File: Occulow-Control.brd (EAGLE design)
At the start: 38.1 x 101.6 mm, 40 parts, among them T1 DMP3010LK3, T2 DMP3010LK3, T3 DMP3010LK3

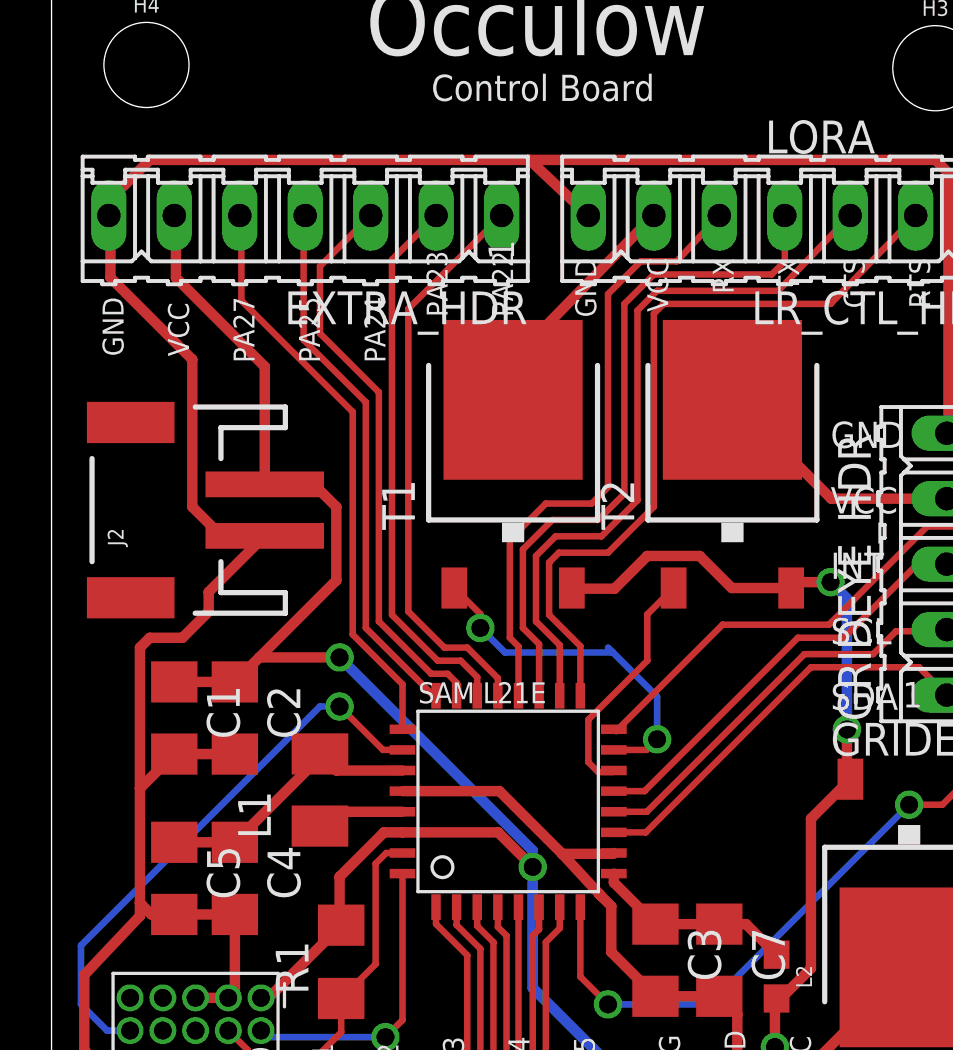
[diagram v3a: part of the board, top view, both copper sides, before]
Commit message: Added LED status, bom. Fixes #6"
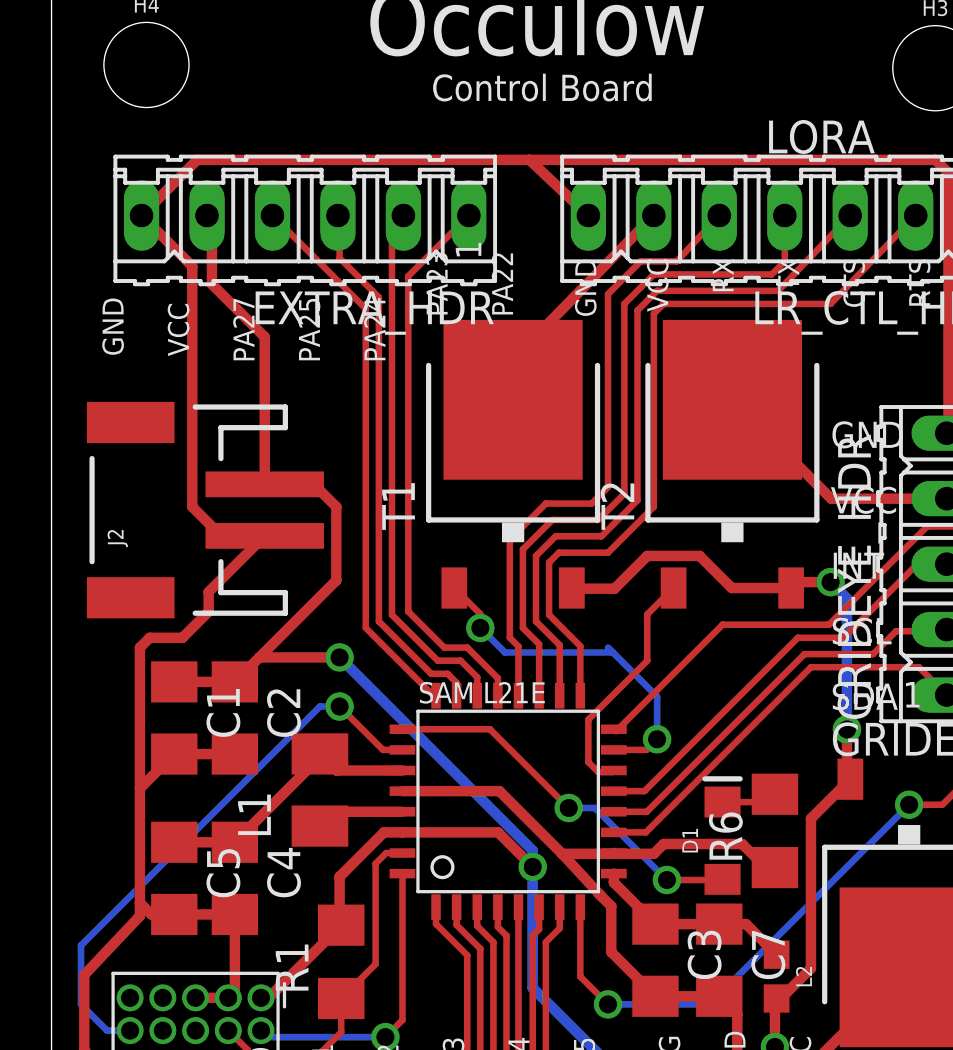
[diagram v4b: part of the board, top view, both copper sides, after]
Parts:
- added D1: (no value), SparkFun-LED:LED-1206
- added R6: 330, resistor:R1206
- EXTRA_HDR: device con-amp-quick:07P -> con-amp-quick:06P
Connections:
- new net N$1: D1.C, R6.2
- net GND: now also EXTRA_HDR.6, R6.1; no longer EXTRA_HDR.7
- net PA27: now also D1.A; no longer EXTRA_HDR.5
- net VCC: now also EXTRA_HDR.5; no longer EXTRA_HDR.6
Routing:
- net PA27: track 22.5 -> 14.9 mm, vias 0 -> 2
- net GND: track 155.6 -> 160.3 mm
- net N$1: track 0.00 -> 2.16 mm
- net PA24: track 22.0 -> 20.9 mm
- net PA25: track 20.8 -> 21.6 mm
- net PA23: track 21.2 -> 20.7 mm
- net VCC: track 101.6 -> 101.1 mm
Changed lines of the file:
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@@
 </element>
 <element name="R1" library="resistor" package="R1206" value="1k" x="11.2395" y="11.049" rot="R90"/>
-<element name="EXTRA_HDR" library="con-amp-quick" package="07P" value="" x="9.8425" y="40.005" rot="R180">
+<element name="EXTRA_HDR" library="con-amp-quick" package="06P" value="" x="9.8425" y="40.005" rot="R180">
 <attribute name="MF" value="" x="9.8425" y="40.005" size="1.778" layer="27" rot="R180" display="off"/>
 <attribute name="MPN" value="" x="9.8425" y="40.005" size="1.778" layer="27" rot="R180" display="off"/>
@@
 </element>
 <element name="U$5" library="cortex-debug" package="2X5-1.27MM" value="CORTEX-ICE" x="5.588" y="9.652" rot="R180"/>
+<element name="D1" library="SparkFun-LED" package="LED-1206" value="" x="26.035" y="15.748" rot="R90"/>
+<element name="R6" library="resistor" package="R1206" value="330" x="28.067" y="16.129" rot="R90"/>
 </elements>
 <signals>
@@
 <contactref element="C1" pad="2"/>
 <contactref element="C2" pad="2"/>
-<contactref element="EXTRA_HDR" pad="7"/>
 <contactref element="C4" pad="2"/>
 <contactref element="C5" pad="2"/>
@@
 <wire x1="17.38" y1="17.672" x2="19.812" y2="15.24" width="0.4064" layer="1"/>
 <wire x1="19.812" y1="15.24" x2="21.7845" y2="15.24" width="0.4064" layer="1"/>
-<wire x1="21.7845" y1="15.24" x2="21.8165" y2="15.272" width="0.4064" layer="1"/>
+<wire x1="21.8165" y1="15.272" x2="21.7845" y2="15.24" width="0.4064" layer="1"/>
 <wire x1="19.812" y1="15.24" x2="21.262965625" y2="13.668121875" width="0.4064" layer="1"/>
 <wire x1="21.262965625" y1="13.668121875" x2="21.336" y2="13.589" width="0.4064" layer="1"/>
@@
 <wire x1="8.272" y1="27.575" x2="6.588" y2="27.575" width="0.4064" layer="1"/>
 <wire x1="6.588" y1="27.575" x2="5.461" y2="28.702" width="0.4064" layer="1"/>
-<wire x1="5.461" y1="28.702" x2="5.461" y2="34.417" width="0.4064" layer="1"/>
-<wire x1="5.461" y1="34.417" x2="2.286" y2="37.592" width="0.4064" layer="1"/>
-<wire x1="2.286" y1="37.592" x2="2.286" y2="39.9415" width="0.4064" layer="1"/>
-<wire x1="2.286" y1="39.9415" x2="2.2225" y2="40.005" width="0.4064" layer="1"/>
-<wire x1="2.2225" y1="40.005" x2="2.2225" y2="40.5765" width="0.4064" layer="1"/>
-<wire x1="2.2225" y1="40.5765" x2="3.81" y2="42.164" width="0.4064" layer="1"/>
-<wire x1="3.81" y1="42.164" x2="18.542" y2="42.164" width="0.4064" layer="1"/>
-<wire x1="18.542" y1="42.164" x2="20.828" y2="40.005" width="0.4064" layer="1"/>
+<wire x1="20.828" y1="40.005" x2="18.542" y2="42.164" width="0.4064" layer="1"/>
 <wire x1="3.429" y1="13.335" x2="3.429" y2="12.827" width="0.4064" layer="1"/>
 <wire x1="3.429" y1="12.827" x2="1.27" y2="10.541" width="0.4064" layer="1"/>
@@
 <wire x1="7.112" y1="9.906" x2="6.858" y2="9.652" width="0.4064" layer="1"/>
 <wire x1="6.858" y1="9.652" x2="5.588" y2="9.652" width="0.4064" layer="1"/>
+<contactref element="R6" pad="1"/>
+<contactref element="EXTRA_HDR" pad="6"/>
+<wire x1="28.067" y1="14.707" x2="27.711" y2="14.707" width="0.4064" layer="1"/>
+<wire x1="27.711" y1="14.707" x2="26.797" y2="15.621" width="0.4064" layer="1"/>
+<wire x1="26.797" y1="15.621" x2="23.749" y2="15.621" width="0.4064" layer="1"/>
+<wire x1="23.749" y1="15.621" x2="23.368" y2="15.24" width="0.4064" layer="1"/>
+<wire x1="23.368" y1="15.24" x2="21.8485" y2="15.24" width="0.4064" layer="1"/>
+<wire x1="21.8485" y1="15.24" x2="21.8165" y2="15.272" width="0.4064" layer="1"/>
+<wire x1="3.4925" y1="40.005" x2="5.461" y2="38.0365" width="0.4064" layer="1"/>
+<wire x1="5.461" y1="28.702" x2="5.461" y2="38.0365" width="0.4064" layer="1"/>
+<wire x1="18.542" y1="42.164" x2="5.6515" y2="42.164" width="0.4064" layer="1"/>
+<wire x1="5.6515" y1="42.164" x2="3.4925" y2="40.005" width="0.4064" layer="1"/>
 </signal>
 <signal name="VCC">
@@
 <contactref element="U$1" pad="30"/>
 <contactref element="C2" pad="1"/>
-<contactref element="EXTRA_HDR" pad="6"/>
 <wire x1="7.112" y1="21.9105" x2="4.7625" y2="21.9105" width="0.4064" layer="1"/>
-<wire x1="8.272" y1="34.146" x2="8.272" y2="29.575" width="0.4064" layer="1"/>
-<wire x1="8.272" y1="34.146" x2="4.826" y2="37.592" width="0.4064" layer="1"/>
-<wire x1="4.826" y1="37.592" x2="4.826" y2="39.9415" width="0.4064" layer="1"/>
-<wire x1="4.826" y1="39.9415" x2="4.7625" y2="40.005" width="0.4064" layer="1"/>
 <wire x1="17.329" y1="16.072" x2="13.6165" y2="16.072" width="0.4064" layer="1"/>
 <wire x1="17.329" y1="16.072" x2="18.669" y2="14.732" width="0.4064" layer="1"/>
@@
 <wire x1="29.464" y1="10.795" x2="29.464" y2="16.605" width="0.4064" layer="1"/>
 <wire x1="30.994" y1="18.135" x2="29.464" y2="16.605" width="0.4064" layer="1"/>
-<wire x1="8.272" y1="29.575" x2="10.176" y2="29.575" width="0.4064" layer="1"/>
+<wire x1="10.176" y1="29.575" x2="8.272" y2="29.575" width="0.4064" layer="1"/>
 <wire x1="10.176" y1="29.575" x2="11.049" y2="28.702" width="0.4064" layer="1"/>
 <wire x1="11.049" y1="28.702" x2="11.049" y2="25.8475" width="0.4064" layer="1"/>
@@
 <wire x1="11.176" y1="22.86" x2="8.0615" y2="22.86" width="0.4064" layer="1"/>
 <wire x1="18.669" y1="15.367" x2="11.176" y2="22.86" width="0.4064" layer="16"/>
+<contactref element="EXTRA_HDR" pad="5"/>
+<wire x1="8.272" y1="35.289" x2="6.223" y2="37.338" width="0.4064" layer="1"/>
+<wire x1="6.223" y1="37.338" x2="6.223" y2="39.8145" width="0.4064" layer="1"/>
+<wire x1="6.223" y1="39.8145" x2="6.0325" y2="40.005" width="0.4064" layer="1"/>
+<wire x1="8.272" y1="29.575" x2="8.272" y2="35.289" width="0.4064" layer="1"/>
 </signal>
 <signal name="RF">
@@
 <wire x1="16.129" y1="23.241" x2="15.24" y2="23.241" width="0.254" layer="1"/>
 <wire x1="15.24" y1="23.241" x2="13.843" y2="24.638" width="0.254" layer="1"/>
-<wire x1="13.843" y1="24.638" x2="13.843" y2="36.3855" width="0.254" layer="1"/>
-<wire x1="13.843" y1="36.3855" x2="17.4625" y2="40.005" width="0.254" layer="1"/>
+<wire x1="13.843" y1="24.638" x2="13.843" y2="36.322" width="0.254" layer="1"/>
+<wire x1="13.843" y1="36.322" x2="13.843" y2="36.3855" width="0.254" layer="1"/>
+<wire x1="13.843" y1="36.322" x2="13.843" y2="37.6555" width="0.254" layer="1"/>
+<wire x1="13.843" y1="37.6555" x2="16.1925" y2="40.005" width="0.254" layer="1"/>
 </signal>
 <signal name="PA23">
@@
 <wire x1="15.875" y1="22.733" x2="14.986" y2="22.733" width="0.254" layer="1"/>
 <wire x1="14.986" y1="22.733" x2="13.208" y2="24.511" width="0.254" layer="1"/>
-<wire x1="13.208" y1="24.511" x2="13.208" y2="38.2905" width="0.254" layer="1"/>
-<wire x1="13.208" y1="38.2905" x2="14.9225" y2="40.005" width="0.254" layer="1"/>
+<wire x1="13.208" y1="39.5605" x2="13.6525" y2="40.005" width="0.254" layer="1"/>
+<wire x1="13.208" y1="24.511" x2="13.208" y2="39.5605" width="0.254" layer="1"/>
 </signal>
 <signal name="PIR_TRIG">
@@
 <signal name="PA27">
 <contactref element="U$1" pad="25"/>
-<contactref element="EXTRA_HDR" pad="5"/>
-<wire x1="13.6165" y1="20.072" x2="13.6165" y2="21.8165" width="0.254" layer="1"/>
-<wire x1="13.6165" y1="21.8165" x2="11.684" y2="23.749" width="0.254" layer="1"/>
-<wire x1="11.684" y1="23.749" x2="11.684" y2="32.385" width="0.254" layer="1"/>
-<wire x1="11.684" y1="32.385" x2="7.366" y2="36.703" width="0.254" layer="1"/>
-<wire x1="7.366" y1="36.703" x2="7.366" y2="39.9415" width="0.254" layer="1"/>
-<wire x1="7.366" y1="39.9415" x2="7.3025" y2="40.005" width="0.254" layer="1"/>
+<contactref element="D1" pad="A"/>
+<wire x1="13.6165" y1="20.072" x2="17.012" y2="20.072" width="0.254" layer="1"/>
+<wire x1="17.012" y1="20.072" x2="20.066" y2="17.018" width="0.254" layer="1"/>
+<via x="20.066" y="17.018" extent="1-16" drill="0.7"/>
+<wire x1="20.066" y1="17.018" x2="21.082" y2="17.018" width="0.254" layer="16"/>
+<wire x1="21.082" y1="17.018" x2="23.876" y2="14.224" width="0.254" layer="16"/>
+<via x="23.876" y="14.224" extent="1-16" drill="0.7"/>
+<wire x1="23.876" y1="14.224" x2="26.011" y2="14.224" width="0.254" layer="1"/>
+<wire x1="26.011" y1="14.224" x2="26.035" y2="14.248" width="0.254" layer="1"/>
 </signal>
 <signal name="SWDIO">
@@
 <wire x1="15.367" y1="22.225" x2="14.732" y2="22.225" width="0.254" layer="1"/>
 <wire x1="14.732" y1="22.225" x2="12.7" y2="24.257" width="0.254" layer="1"/>
-<wire x1="12.7" y1="24.257" x2="12.7" y2="33.147" width="0.254" layer="1"/>
-<wire x1="12.7" y1="33.147" x2="10.414" y2="35.433" width="0.254" layer="1"/>
-<wire x1="10.414" y1="35.433" x2="10.414" y2="38.0365" width="0.254" layer="1"/>
-<wire x1="10.414" y1="38.0365" x2="12.3825" y2="40.005" width="0.254" layer="1"/>
+<wire x1="12.7" y1="36.83" x2="11.176" y2="38.354" width="0.254" layer="1"/>
+<wire x1="11.176" y1="38.354" x2="11.176" y2="39.9415" width="0.254" layer="1"/>
+<wire x1="11.176" y1="39.9415" x2="11.1125" y2="40.005" width="0.254" layer="1"/>
+<wire x1="12.7" y1="24.257" x2="12.7" y2="36.83" width="0.254" layer="1"/>
 </signal>
 <signal name="PA25">
@@
 <wire x1="14.9165" y1="21.372" x2="14.823" y2="21.372" width="0.254" layer="1"/>
 <wire x1="14.823" y1="21.372" x2="12.192" y2="24.003" width="0.254" layer="1"/>
-<wire x1="12.192" y1="24.003" x2="12.192" y2="32.766" width="0.254" layer="1"/>
-<wire x1="12.192" y1="32.766" x2="9.779" y2="35.179" width="0.254" layer="1"/>
-<wire x1="9.779" y1="35.179" x2="9.779" y2="39.9415" width="0.254" layer="1"/>
-<wire x1="9.779" y1="39.9415" x2="9.8425" y2="40.005" width="0.254" layer="1"/>
+<wire x1="8.5725" y1="40.005" x2="8.763" y2="39.8145" width="0.254" layer="1"/>
+<wire x1="12.192" y1="36.3855" x2="8.5725" y2="40.005" width="0.254" layer="1"/>
+<wire x1="12.192" y1="24.003" x2="12.192" y2="36.3855" width="0.254" layer="1"/>
 </signal>
 <signal name="VDDCORE">
@@
 <wire x1="30.2495" y1="29.0195" x2="26.416" y2="32.853" width="0.4064" layer="1"/>
 </signal>
+<signal name="N$1">
+<contactref element="R6" pad="2"/>
+<contactref element="D1" pad="C"/>
+<wire x1="26.035" y1="17.248" x2="27.764" y2="17.248" width="0.254" layer="1"/>
+<wire x1="27.764" y1="17.248" x2="28.067" y2="17.551" width="0.254" layer="1"/>
+</signal>
 </signals>

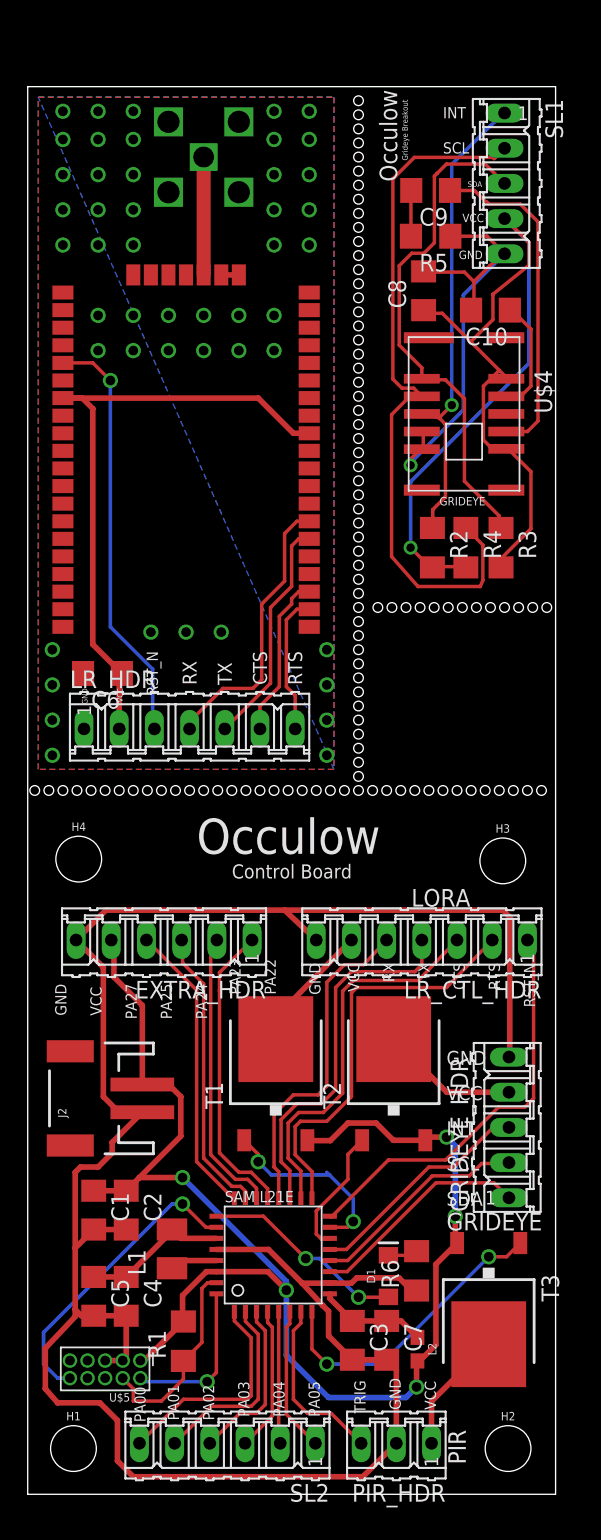
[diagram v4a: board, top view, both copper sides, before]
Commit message: Added vcc pull up for reset and button switch. Fixes #7
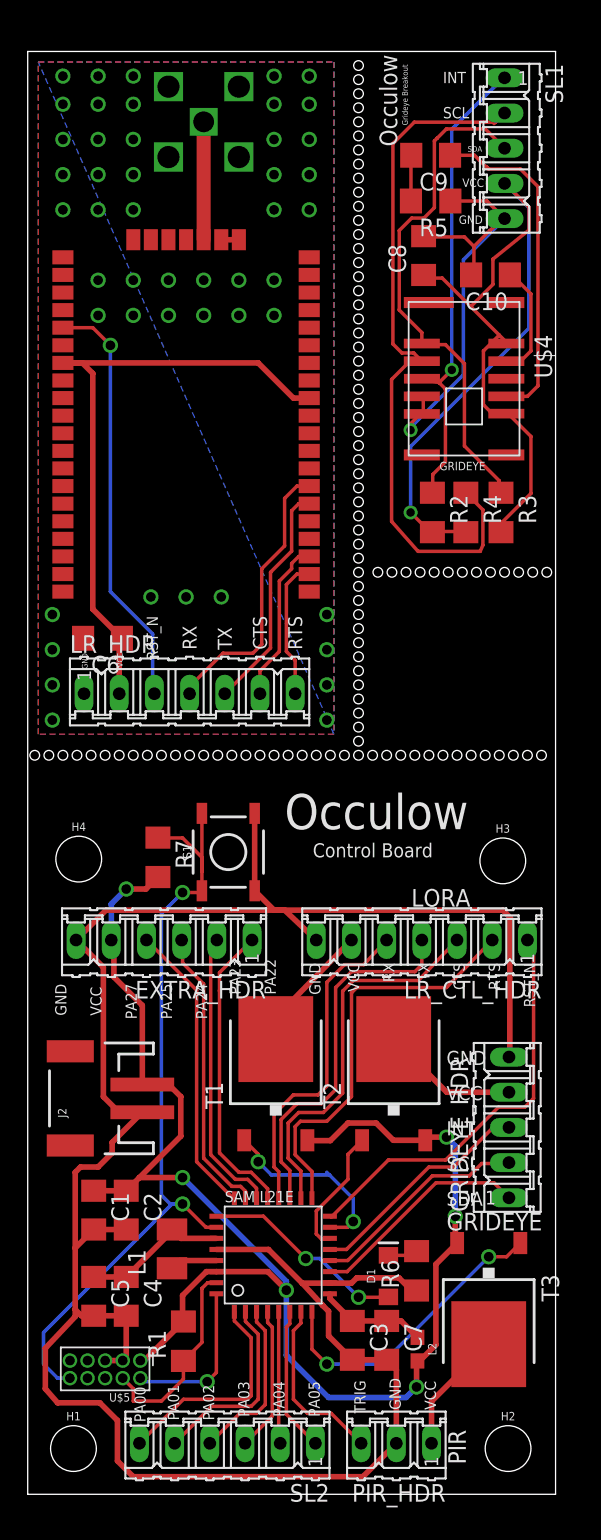
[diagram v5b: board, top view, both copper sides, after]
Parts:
- added R7: 10k, resistor:R1206
- added S1: SWITCH, SparkFun-Switches:TACTILE_SWITCH_SMD_5.2MM
- moved C8 2.54 mm to (28.6, 89.4)
- moved C9 2.54 mm to (29.1, 96.6)
- moved R2 2.54 mm to (29.2, 70.9)
- moved R3 2.54 mm to (34.2, 70.9)
- moved R4 2.54 mm to (31.6, 70.9)
- moved SL1 2.54 mm to (34.4, 97.2)
- moved U$2 2.54 mm to (11.4, 76.6)
- moved U$3 2.54 mm to (12.7, 99.1)
- moved U$4 2.54 mm to (31.5, 80.5)
- moved C6 2.54 mm to (5.40, 61.8)
- moved LR_HDR 2.54 mm to (11.7, 57.8)
- moved C10 2.54 mm to (33.4, 88.0)
- moved R5 2.54 mm to (29.1, 93.3)
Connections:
- net !RESET: now also R7.1, S1.1, S1.2
- net GND: now also S1.3, S1.4
- net VCC: now also R7.2
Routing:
- net !RESET: track 21.6 -> 57.7 mm, vias 1 -> 2
- net GND: track 160.3 -> 168.6 mm
- net VCC: track 101.1 -> 107.9 mm, vias 5 -> 6
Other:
- board size 38.1 x 101.6 mm -> 38.1 x 104.1 mm
